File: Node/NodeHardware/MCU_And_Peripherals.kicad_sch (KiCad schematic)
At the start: 87 parts, among them Q3 2N7002, Q4 2N7002, SW1 RST, SW2 BOOT, SW3 BTN, U6 ESP32-S3-WROOM-1, U7 UCC27511ADBV

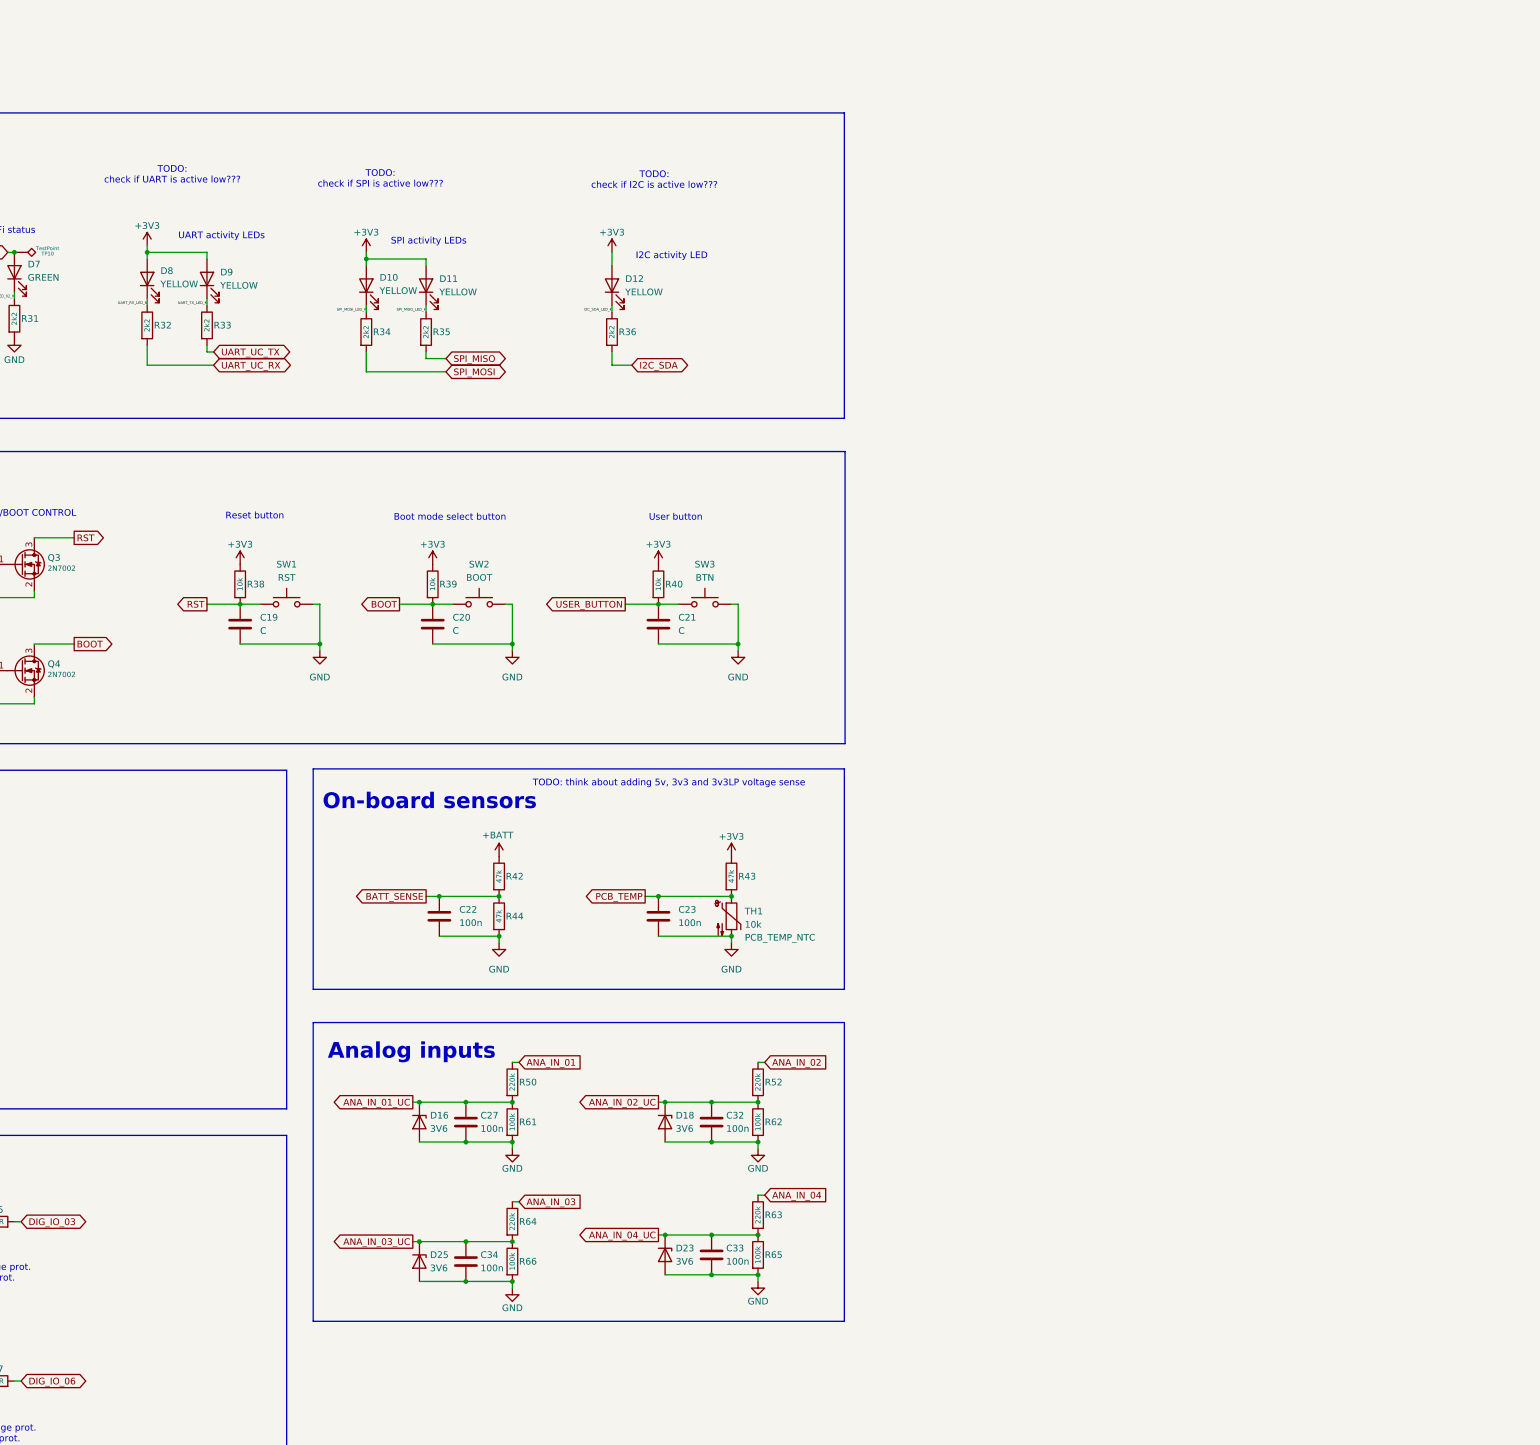
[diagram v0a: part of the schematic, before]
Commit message: added some comments and sim module to schematic
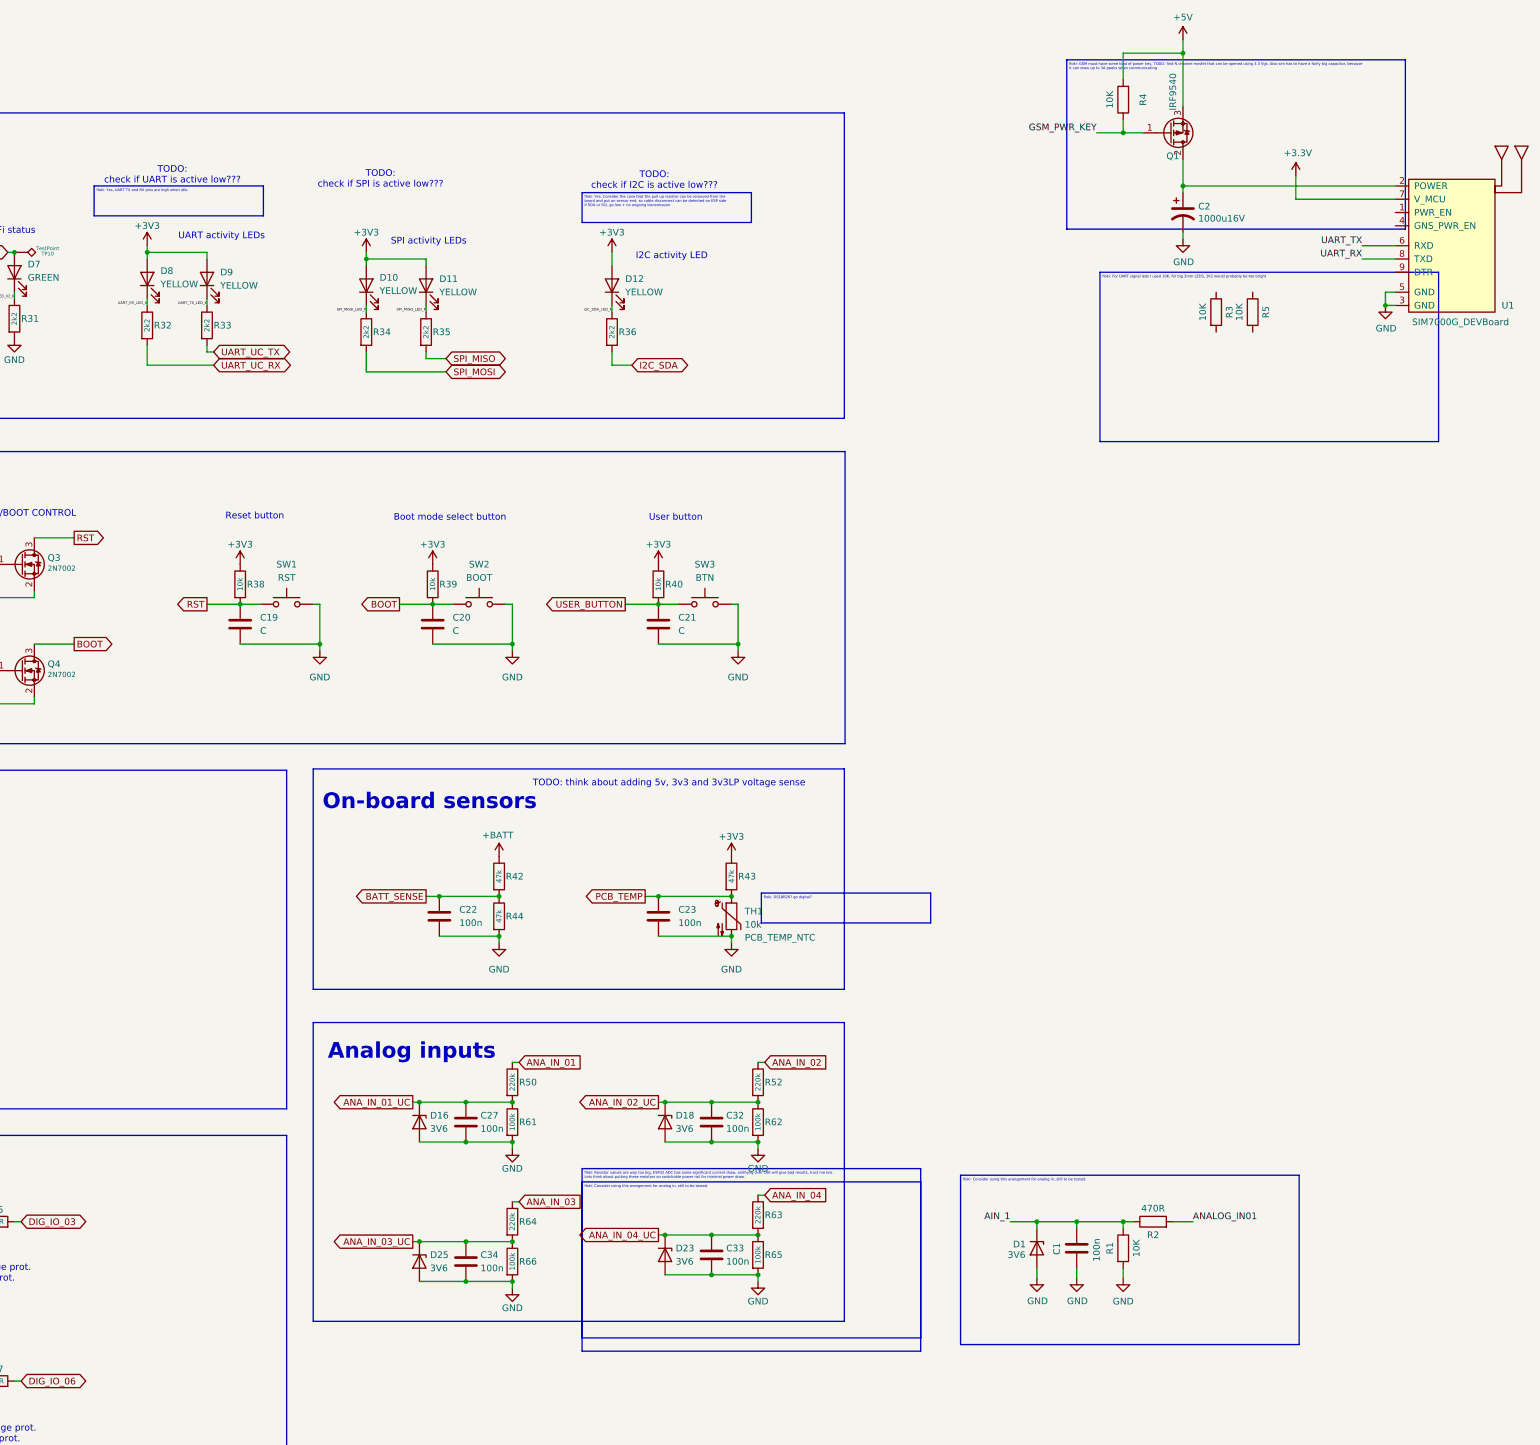
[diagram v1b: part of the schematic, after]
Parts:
- added C1: 100n, Capacitor_SMD:C_1206_3216Metric_Pad1.42x1.75mm_HandSolder, symbol Device:C
- added C2: 1000u16V, myComponents:CAP_Radial_D10.0mm_P5.00mm, symbol Device:CP1
- added D1: 3V6, Diode_SMD:D_SOD-123, symbol Device:D_Zener
- added Q1: IRF9540, myComponents:TO-220-3_SolderedTab, symbol Device:Q_PMOS_GDS
- added R1: 10K, Resistor_SMD:R_0805_2012Metric_Pad1.15x1.40mm_HandSolder, symbol Device:R
- added R2: 470R, Resistor_SMD:R_0805_2012Metric_Pad1.15x1.40mm_HandSolder, symbol Device:R
- added R3, R4, R5: 10K, Resistor_SMD:R_0805_2012Metric_Pad1.20x1.40mm_HandSolder, symbol Device:R
- added U1: SIM7000G_DEVBoard, myComponents:sim7000G_dev_board_rev3, symbol myComponents:SIM7000G_DEVBoard
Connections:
- net GND: now also C1.2, C2.2, D1.2 (A), R1.2, U1.3 (GND), U1.5 (GND)
- new net: C2.1, Q1.2 (D), U1.2 (POWER)
- new net +3.3V: U1.7 (V_MCU)
- new net +5V: Q1.3 (S), R4.2
- new net AIN_1: C1.1, D1.1 (K), R1.1, R2.1
- new net ANALOG_IN01: R2.2
- new net GSM_PWR_KEY: Q1.1 (G), R4.1
- new net UART_RX: U1.8 (TXD)
- new net UART_TX: U1.6 (RXD)
